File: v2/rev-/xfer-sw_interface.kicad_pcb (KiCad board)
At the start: 2 copper layers, 44.4 x 31.8 mm, 51 parts, among them J1 CONTROL, J2 XFER_SW, J3 28VDC_IN, Q1 IRLML9301, Q2 IRLML9301, Q3 IRLML9301, Q4 IRLML9301, Q5 MMBTA06LT1G, Q6 MMBTA06LT1G, U1 ILD207T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

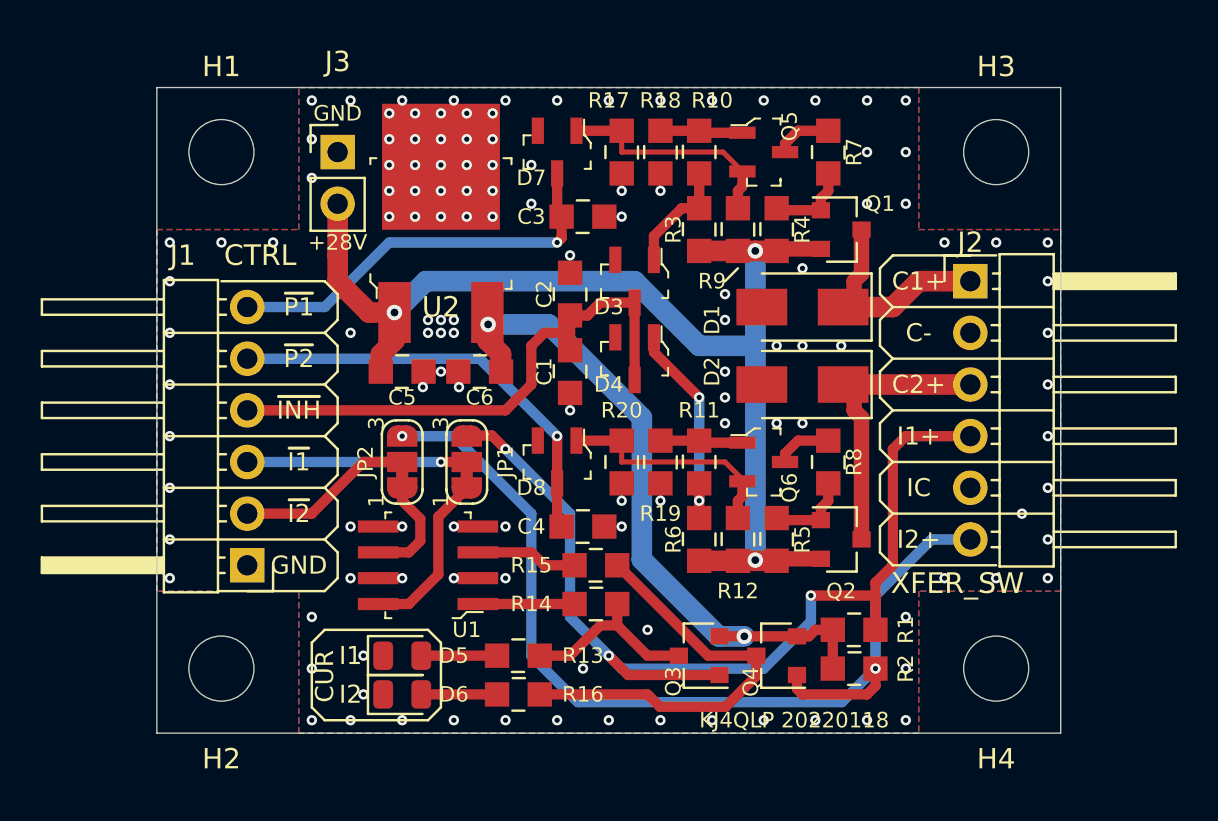
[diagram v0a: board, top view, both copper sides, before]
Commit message: version 2 of xfer switch interface design.  This commit sent to osh park 20220119
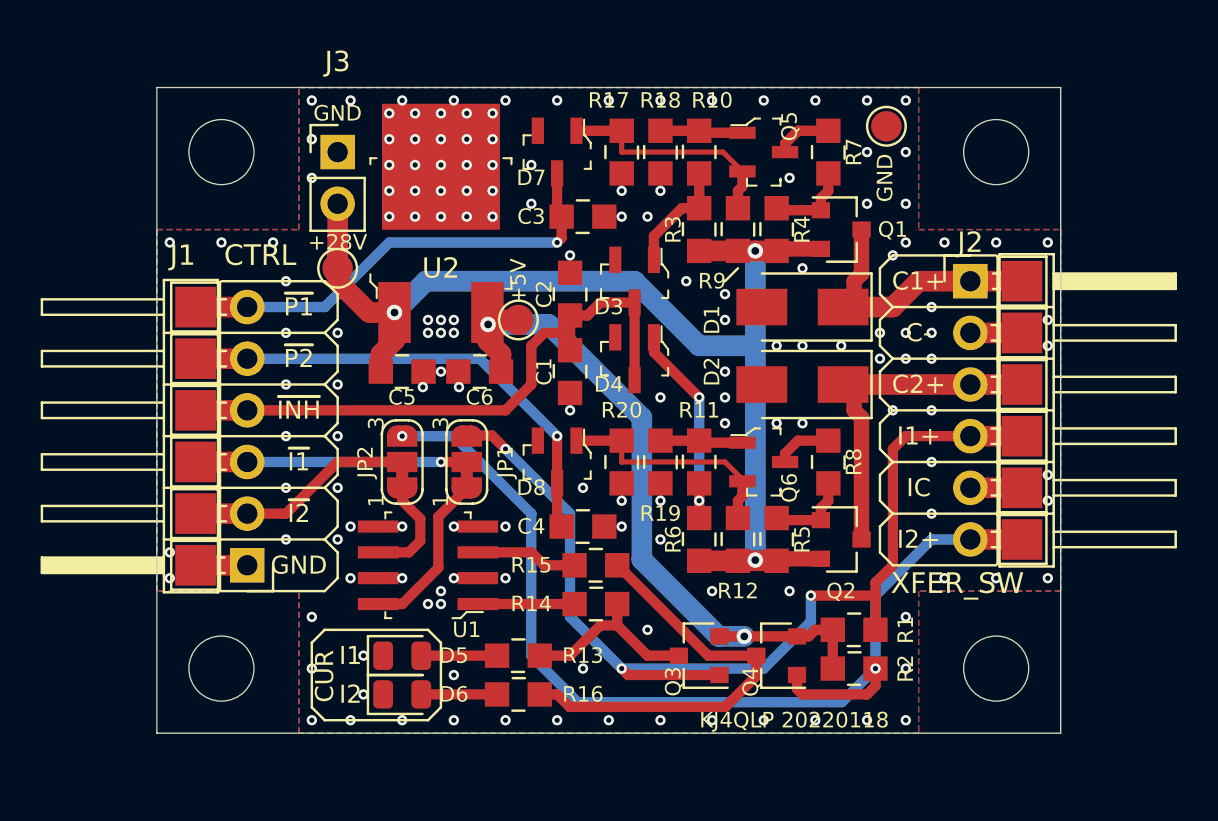
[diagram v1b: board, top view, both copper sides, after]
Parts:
- added TP1: +5V, TestPoint:TestPoint_Pad_D1.5mm, F.Cu at (176.5, 74.9)
- added TP10: ~P1, TestPoint:TestPoint_Pad_2.0x2.0mm, F.Cu at (201.3, 73.0)
- added TP11: ~P2, TestPoint:TestPoint_Pad_2.0x2.0mm, F.Cu at (201.3, 75.6)
- added TP12: ~INH, TestPoint:TestPoint_Pad_2.0x2.0mm, F.Cu at (201.3, 78.1)
- added TP13: ~I1_CTL, TestPoint:TestPoint_Pad_2.0x2.0mm, F.Cu at (201.3, 80.6)
- added TP14: ~I2_CTL, TestPoint:TestPoint_Pad_2.0x2.0mm, F.Cu at (201.3, 83.2)
- added TP15: GND, TestPoint:TestPoint_Pad_2.0x2.0mm, F.Cu at (201.3, 85.7)
- added TP2: +28V, TestPoint:TestPoint_Pad_D1.5mm, F.Cu at (167.6, 72.4)
- added TP3: GND, TestPoint:TestPoint_Pad_D1.5mm, F.Cu at (194.6, 65.4)
- added TP4: ~P1, TestPoint:TestPoint_Pad_2.0x2.0mm, F.Cu at (160.7, 74.3)
- added TP5: ~P2, TestPoint:TestPoint_Pad_2.0x2.0mm, F.Cu at (160.7, 76.8)
- added TP6: ~INH, TestPoint:TestPoint_Pad_2.0x2.0mm, F.Cu at (160.7, 79.4)
- added TP7: ~I1_CTL, TestPoint:TestPoint_Pad_2.0x2.0mm, F.Cu at (160.7, 81.9)
- added TP8: ~I2_CTL, TestPoint:TestPoint_Pad_2.0x2.0mm, F.Cu at (160.7, 84.5)
- added TP9: GND, TestPoint:TestPoint_Pad_2.0x2.0mm, F.Cu at (160.7, 87.0)
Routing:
- net GND: track 0.00 -> 7.62 mm, vias 127 -> 154
- net ~P2: track 21.4 -> 23.9 mm
- net ~P1: track 20.1 -> 22.7 mm
- net ~INH: track 27.5 -> 30.1 mm
- net ~I2_CTL: track 8.67 -> 11.2 mm
- net ~I1_CTL: track 10.8 -> 13.3 mm
- net I2: track 48.6 -> 51.1 mm
- net C1+: track 11.0 -> 13.5 mm
- net C2+: track 14.2 -> 16.8 mm
- net +5V: track 34.4 -> 36.1 mm
- net I1: track 49.2 -> 50.9 mm
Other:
- board text added: "+5V"
- board text added: "Transfer Switch Interface w/ Indicator Feedback VTGS SX-Band System Version 2, Revision- KJ4QLP, 20220118"
- board text removed: "XFER Switch Interface w/ Indicator Feedback VTGS SX-Band System Version 2, Revision- KJ4QLP, 20220118"
